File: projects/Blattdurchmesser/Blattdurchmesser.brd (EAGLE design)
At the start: 100 x 80 mm, 16 parts, among them K1 TX2_RELAY", Q1 ARDUINOR3-NOIOREF-NOTEXT

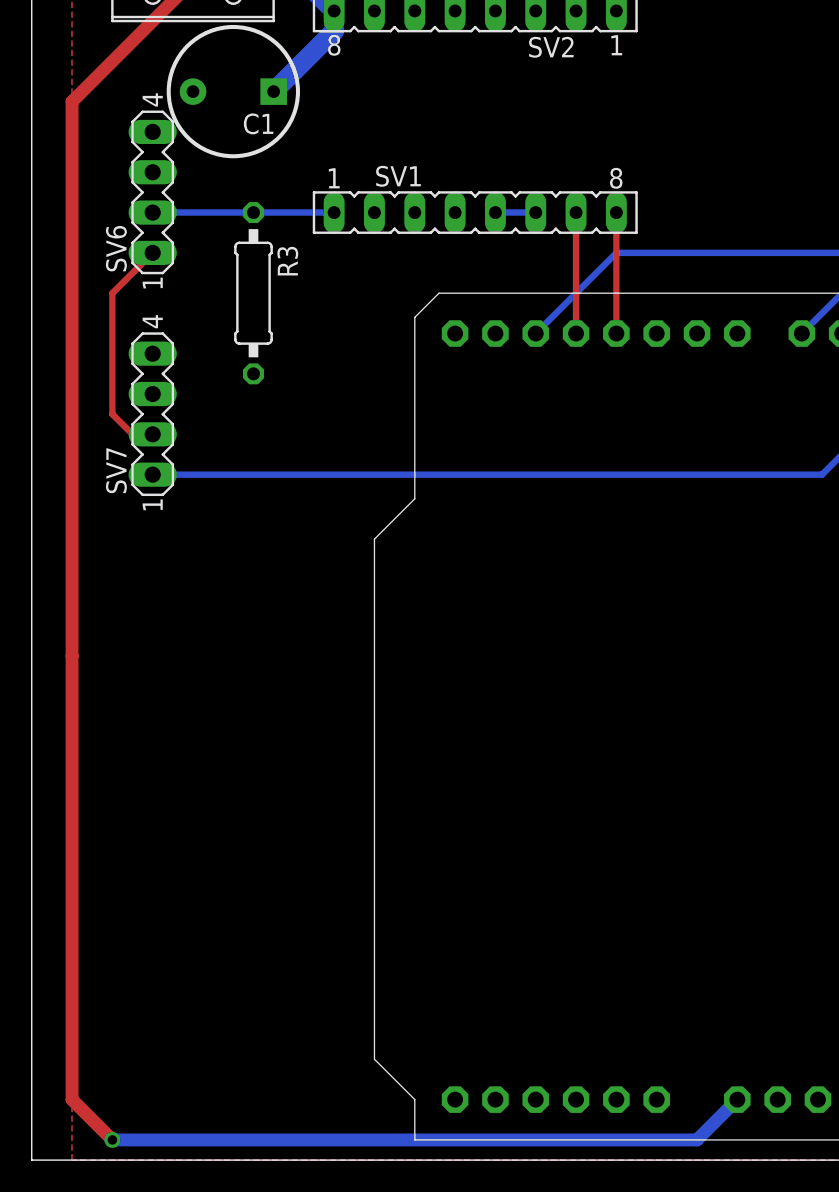
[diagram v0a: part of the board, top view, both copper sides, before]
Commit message: bugfix; * edrc dimension errors
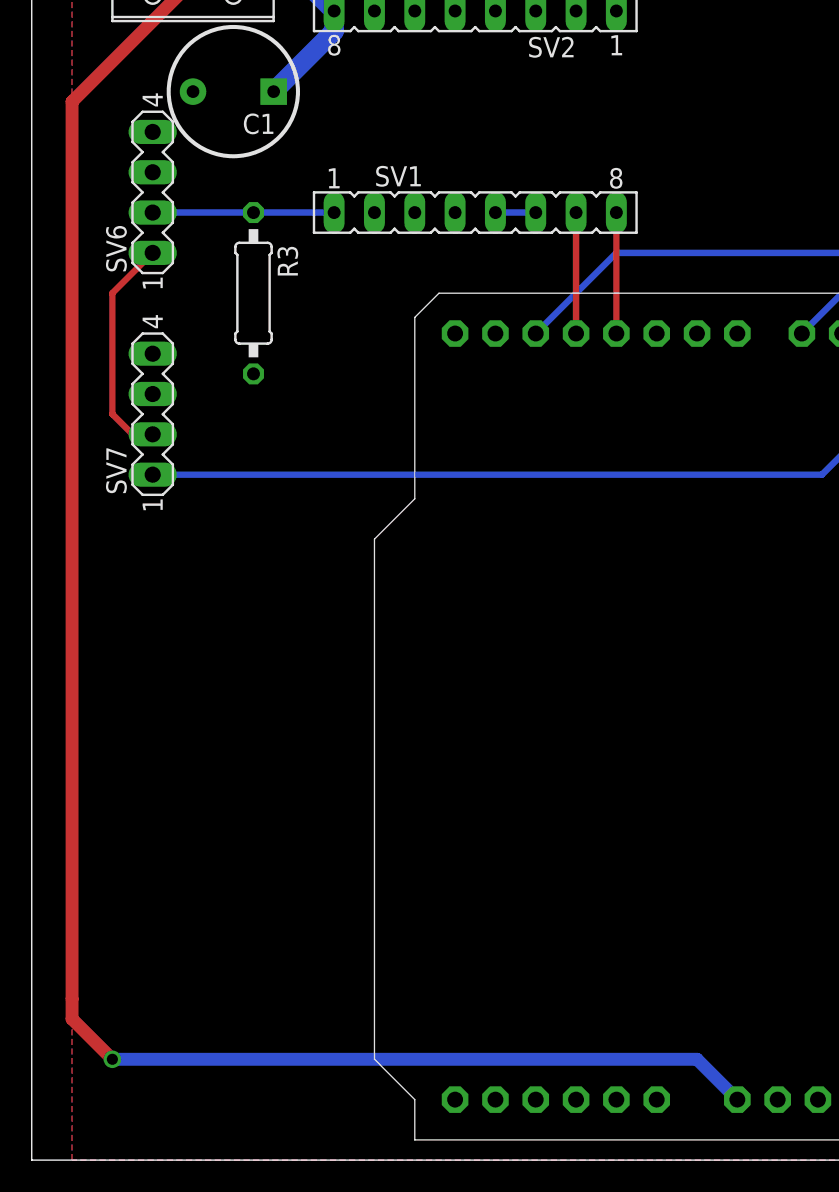
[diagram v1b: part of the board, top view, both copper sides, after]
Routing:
- net +12V: track 136.1 -> 131.0 mm
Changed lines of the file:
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@@
 <wire x1="19.05" y1="72.39" x2="19.05" y2="71.12" width="1.2192" layer="16"/>
 <wire x1="19.05" y1="71.12" x2="15.24" y2="67.31" width="1.2192" layer="16"/>
-<wire x1="2.54" y1="31.75" x2="2.54" y2="66.675" width="0.8128" layer="1"/>
+<wire x1="2.54" y1="10.16" x2="2.54" y2="66.675" width="0.8128" layer="1"/>
 <wire x1="2.54" y1="66.675" x2="12.7" y2="76.835" width="0.8128" layer="1"/>
 <contactref element="Q1" pad="VIN"/>
-<wire x1="2.54" y1="31.75" x2="2.54" y2="3.81" width="0.8128" layer="1"/>
-<wire x1="2.54" y1="3.81" x2="5.08" y2="1.27" width="0.8128" layer="1"/>
-<via x="5.08" y="1.27" extent="1-16" drill="0.6"/>
-<wire x1="5.08" y1="1.27" x2="41.91" y2="1.27" width="0.8128" layer="16"/>
-<wire x1="41.91" y1="1.27" x2="44.45" y2="3.81" width="0.8128" layer="16"/>
+<wire x1="44.45" y1="3.81" x2="41.91" y2="6.35" width="0.8128" layer="16"/>
+<wire x1="41.91" y1="6.35" x2="5.08" y2="6.35" width="0.8128" layer="16"/>
+<via x="5.08" y="6.35" extent="1-16" drill="0.7"/>
+<wire x1="5.08" y1="6.35" x2="2.54" y2="8.89" width="0.8128" layer="1"/>
+<wire x1="2.54" y1="8.89" x2="2.54" y2="10.16" width="0.8128" layer="1"/>
 </signal>
 <signal name="N$3">

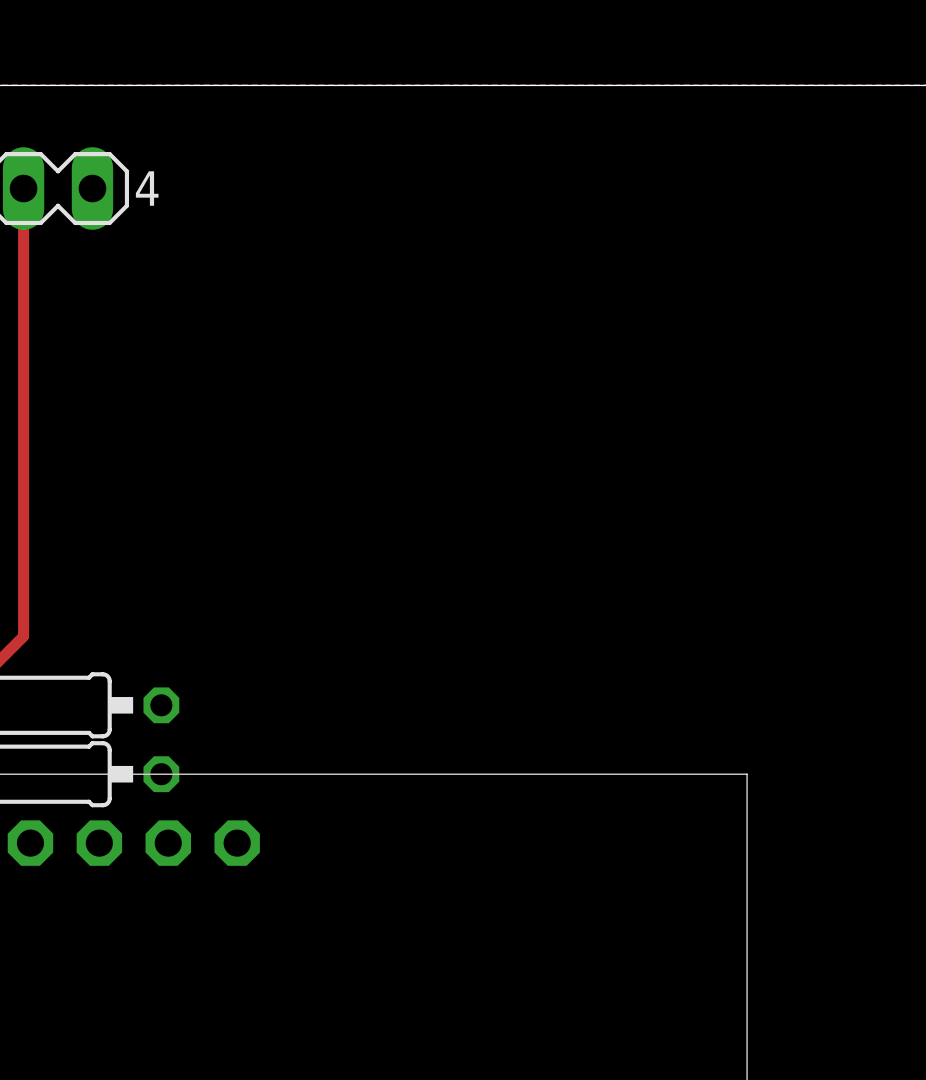
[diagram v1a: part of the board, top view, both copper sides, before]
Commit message: new feature; * add i2c OLED display
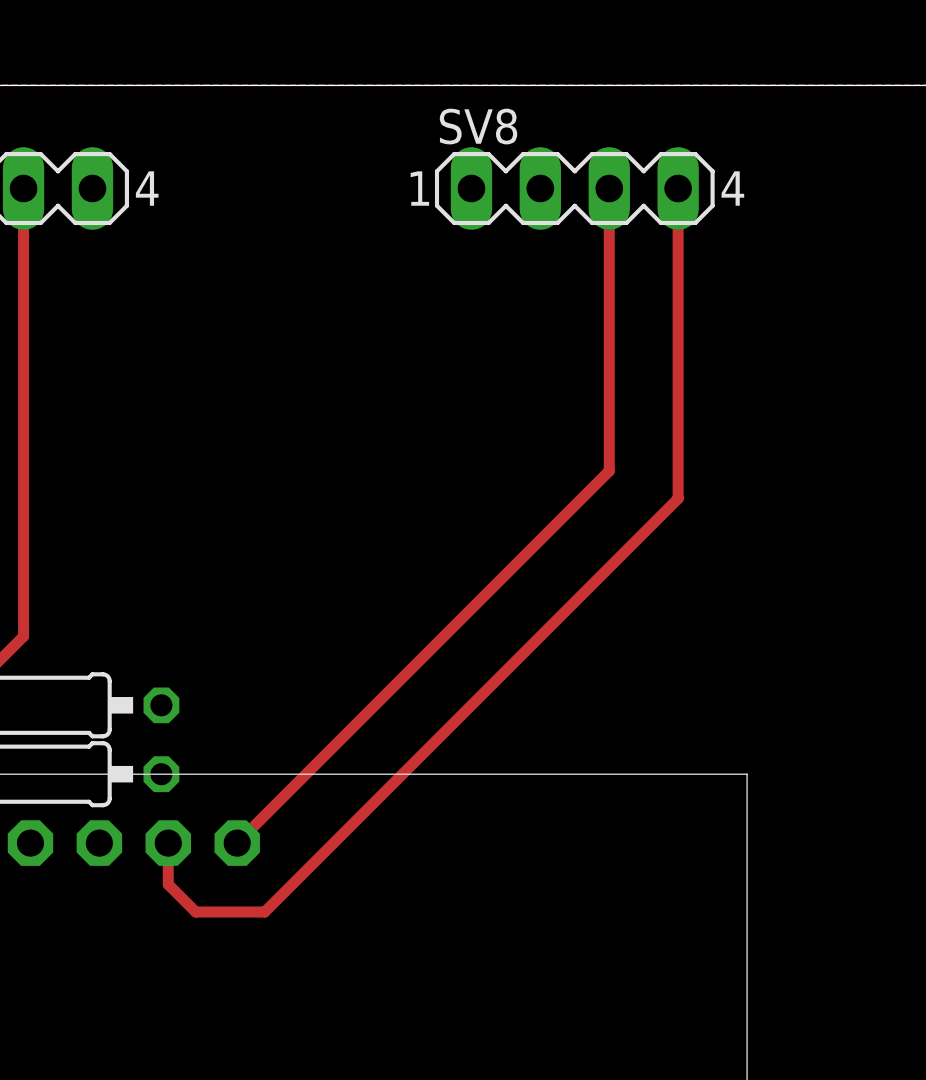
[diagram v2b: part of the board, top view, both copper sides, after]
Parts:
- added SV8: (no value), con-lstb:MA04-1
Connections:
- new net N$17: Q1.SCL, SV8.3
- new net N$18: Q1.SDA, SV8.4
- net +5V: now also SV8.2
- net GND: now also SV8.1
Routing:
- net N$18: track 0.00 -> 38.5 mm
- net N$17: track 0.00 -> 29.8 mm
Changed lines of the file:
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@@
 <attribute name="MF" value="" x="10.16" y="76.2" size="1.778" layer="27" rot="R180" display="off"/>
+</element>
+<element name="SV8" library="con-lstb" package="MA04-1" value="" x="83.82" y="76.2">
+<attribute name="MPN" value="" x="83.82" y="76.2" size="1.778" layer="27" display="off"/>
+<attribute name="OC_FARNELL" value="unknown" x="83.82" y="76.2" size="1.778" layer="27" display="off"/>
+<attribute name="MF" value="" x="83.82" y="76.2" size="1.778" layer="27" display="off"/>
+<attribute name="OC_NEWARK" value="unknown" x="83.82" y="76.2" size="1.778" layer="27" display="off"/>
 </element>
 </elements>
@@
 <contactref element="Q1" pad="GND"/>
 <contactref element="X1" pad="2"/>
+<contactref element="SV8" pad="1"/>
 </signal>
 <signal name="GND1">
@@
 <contactref element="R3" pad="2"/>
 <contactref element="Q1" pad="5V"/>
+<contactref element="SV8" pad="2"/>
 </signal>
 <signal name="+12V">
@@
 <wire x1="6.35" y1="45.72" x2="5.08" y2="46.99" width="0.4064" layer="1"/>
 </signal>
+<signal name="N$17">
+<contactref element="SV8" pad="3"/>
+<contactref element="Q1" pad="SCL"/>
+<wire x1="85.09" y1="76.2" x2="85.09" y2="65.786" width="0.4064" layer="1"/>
+<wire x1="85.09" y1="65.786" x2="71.374" y2="52.07" width="0.4064" layer="1"/>
+</signal>
+<signal name="N$18">
+<contactref element="SV8" pad="4"/>
+<contactref element="Q1" pad="SDA"/>
+<wire x1="87.63" y1="76.2" x2="87.63" y2="64.77" width="0.4064" layer="1"/>
+<wire x1="87.63" y1="64.77" x2="72.39" y2="49.53" width="0.4064" layer="1"/>
+<wire x1="72.39" y1="49.53" x2="69.85" y2="49.53" width="0.4064" layer="1"/>
+<wire x1="69.85" y1="49.53" x2="68.834" y2="50.546" width="0.4064" layer="1"/>
+<wire x1="68.834" y1="50.546" x2="68.834" y2="52.07" width="0.4064" layer="1"/>
+</signal>
 </signals>

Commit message: improvement; * rearranged schematic              * rearranged pcb
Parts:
- moved SV5 17.8 mm to (66.0, 76.2)
- moved SV4 10.2 mm to (52.1, 76.2)
- moved R1 7.62 mm to (55.9, 57.1)
- moved R2 7.62 mm to (55.9, 54.6)
- moved SV8 3.81 mm to (80.0, 76.2)
- moved R3 1.27 mm to (12.7, 54.6)
- moved SV6 1.27 mm to (6.35, 61.0)
- moved SV7 1.27 mm to (6.35, 47.0)
- moved C1 1.27 mm to (14.0, 66.0)
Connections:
- net N$15: now also Q1.A0
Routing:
- net N$15: track 48.9 -> 91.6 mm
- net N$13: track 24.6 -> 36.2 mm, vias 0 -> 1
- net N$9: track 34.7 -> 26.1 mm
- net N$12: track 35.8 -> 28.8 mm
- net N$18: track 38.5 -> 36.9 mm
- net N$17: track 29.8 -> 28.2 mm
- net N$14: track 11.4 -> 12.7 mm
- net N$11: track 54.7 -> 56.0 mm
- net +12V: track 131.0 -> 132.3 mm

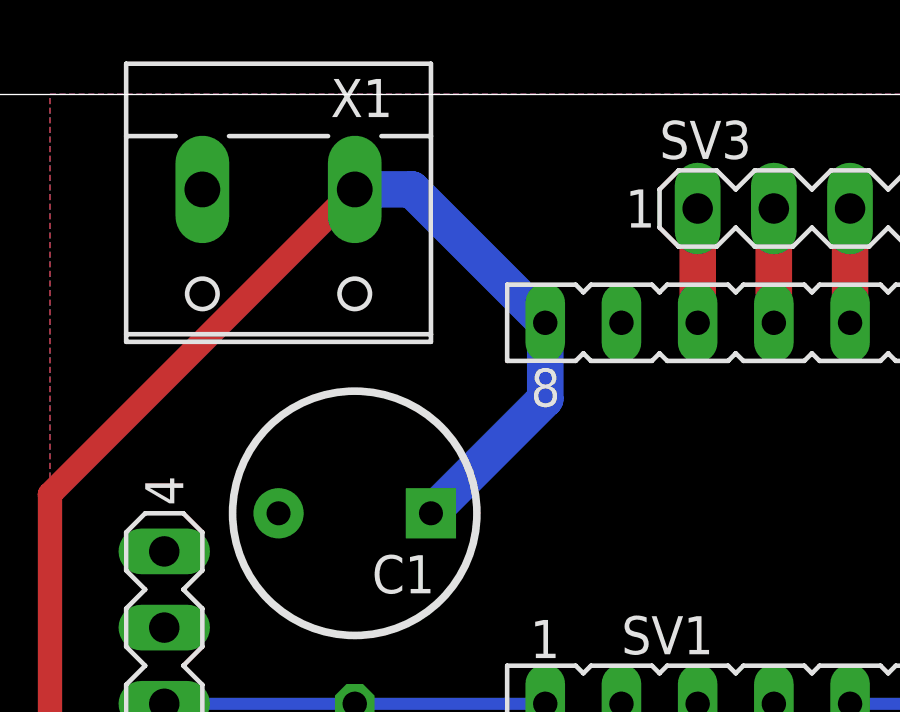
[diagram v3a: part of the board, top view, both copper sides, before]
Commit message: improvement; * move stepper power line to top plane              * add labels to connectors
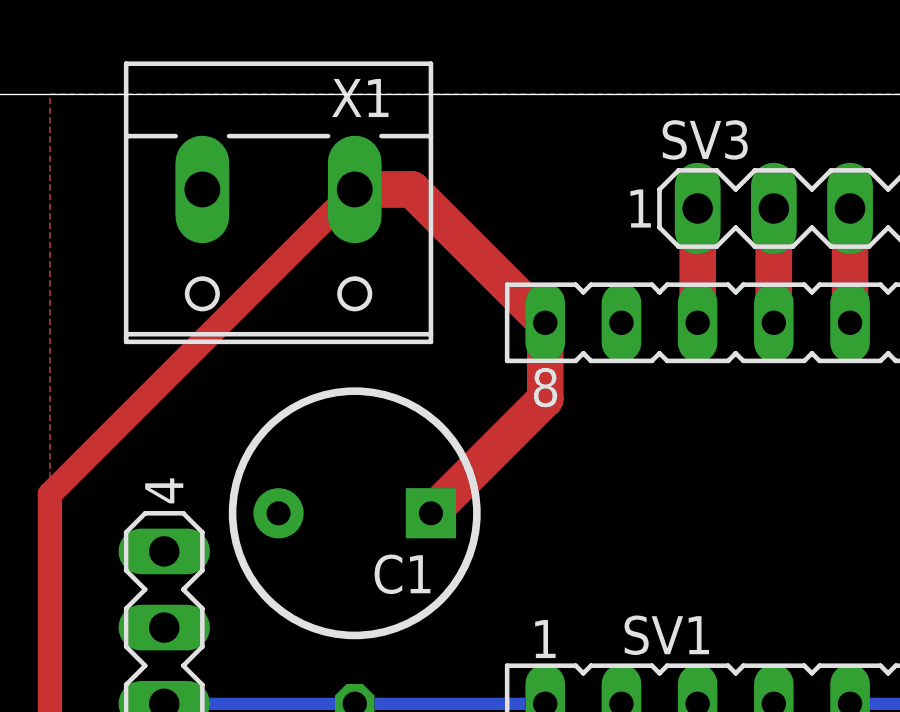
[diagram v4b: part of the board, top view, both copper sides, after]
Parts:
- SV1, SV2: value (none) -> A4988
- SV3: value (none) -> stepper
- SV4: value (none) -> optical
- SV5: value (none) -> mechanical
- SV6: value (none) -> protect2
- SV7: value (none) -> protect1
- SV8: value (none) -> OLED
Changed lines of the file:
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@@
 <elements>
 <element name="K1" library="relay" package="TX2" value="TX2_RELAY&quot;" x="72.39" y="17.78"/>
-<element name="SV1" library="con-lsta" package="FE08" value="" x="27.94" y="59.69">
+<element name="SV1" library="con-lsta" package="FE08" value="A4988" x="27.94" y="59.69">
 <attribute name="MPN" value="" x="27.94" y="59.69" size="1.778" layer="27" display="off"/>
 <attribute name="OC_NEWARK" value="unknown" x="27.94" y="59.69" size="1.778" layer="27" display="off"/>
@@
 <attribute name="MF" value="" x="27.94" y="59.69" size="1.778" layer="27" display="off"/>
 </element>
-<element name="SV2" library="con-lsta" package="FE08" value="" x="27.94" y="72.39" rot="R180">
+<element name="SV2" library="con-lsta" package="FE08" value="A4988" x="27.94" y="72.39" rot="R180">
 <attribute name="MPN" value="" x="27.94" y="72.39" size="1.778" layer="27" rot="R180" display="off"/>
 <attribute name="OC_NEWARK" value="unknown" x="27.94" y="72.39" size="1.778" layer="27" rot="R180" display="off"/>
@@
 <attribute name="MF" value="" x="27.94" y="72.39" size="1.778" layer="27" rot="R180" display="off"/>
 </element>
-<element name="SV4" library="con-lstb" package="MA04-1" value="" x="52.07" y="76.2">
+<element name="SV4" library="con-lstb" package="MA04-1" value="optical" x="52.07" y="76.2">
 <attribute name="MPN" value="" x="52.07" y="76.2" size="1.778" layer="27" display="off"/>
 <attribute name="OC_NEWARK" value="unknown" x="52.07" y="76.2" size="1.778" layer="27" display="off"/>
@@
 <attribute name="MF" value="" x="66.04" y="27.94" size="1.778" layer="27" display="off"/>
 </element>
-<element name="SV3" library="con-lstb" package="MA04-1" value="" x="27.94" y="76.2">
+<element name="SV3" library="con-lstb" package="MA04-1" value="stepper" x="27.94" y="76.2">
 <attribute name="MPN" value="" x="27.94" y="76.2" size="1.778" layer="27" display="off"/>
 <attribute name="OC_NEWARK" value="unknown" x="27.94" y="76.2" size="1.778" layer="27" display="off"/>
@@
 </element>
 <element name="C1" library="Elkos" package="R_ELK_8.1" value="R_ELKO_8.1" x="13.97" y="66.04" rot="R180"/>
-<element name="SV5" library="con-lstb" package="MA04-1" value="" x="66.04" y="76.2">
+<element name="SV5" library="con-lstb" package="MA04-1" value="mechanical" x="66.04" y="76.2">
 <attribute name="MPN" value="" x="66.04" y="76.2" size="1.778" layer="27" display="off"/>
 <attribute name="OC_NEWARK" value="unknown" x="66.04" y="76.2" size="1.778" layer="27" display="off"/>
@@
 <element name="R1" library="rcl" package="0207/10" value="1k" x="55.88" y="57.15"/>
 <element name="R2" library="rcl" package="0207/10" value="1k" x="55.88" y="54.61"/>
-<element name="SV6" library="con-lstb" package="MA04-1" value="" x="6.35" y="60.96" rot="R90">
+<element name="SV6" library="con-lstb" package="MA04-1" value="protect2" x="6.35" y="60.96" rot="R90">
 <attribute name="MPN" value="" x="6.35" y="60.96" size="1.778" layer="27" rot="R90" display="off"/>
 <attribute name="OC_NEWARK" value="unknown" x="6.35" y="60.96" size="1.778" layer="27" rot="R90" display="off"/>
@@
 <element name="R3" library="rcl" package="0207/10" value="4.7k" x="12.7" y="54.61" rot="R270"/>
 <element name="Q1" library="adafruit" package="ARDUINOR3-NOTEXT-NOIOREF" value="ARDUINOR3-NOIOREF-NOTEXT" x="90.17" y="1.27" rot="MR0"/>
-<element name="SV7" library="con-lstb" package="MA04-1" value="" x="6.35" y="46.99" rot="R90">
+<element name="SV7" library="con-lstb" package="MA04-1" value="protect1" x="6.35" y="46.99" rot="R90">
 <attribute name="MPN" value="" x="6.35" y="46.99" size="1.778" layer="27" rot="R90" display="off"/>
 <attribute name="OC_FARNELL" value="unknown" x="6.35" y="46.99" size="1.778" layer="27" rot="R90" display="off"/>
@@
 <attribute name="MF" value="" x="10.16" y="76.2" size="1.778" layer="27" rot="R180" display="off"/>
 </element>
-<element name="SV8" library="con-lstb" package="MA04-1" value="" x="80.01" y="76.2">
+<element name="SV8" library="con-lstb" package="MA04-1" value="OLED" x="80.01" y="76.2">
 <attribute name="MPN" value="" x="80.01" y="76.2" size="1.778" layer="27" display="off"/>
 <attribute name="OC_FARNELL" value="unknown" x="80.01" y="76.2" size="1.778" layer="27" display="off"/>
@@
 <contactref element="C1" pad="P"/>
 <contactref element="X1" pad="1"/>
-<wire x1="12.7" y1="76.835" x2="14.605" y2="76.835" width="1.2192" layer="16"/>
-<wire x1="14.605" y1="76.835" x2="19.05" y2="72.39" width="1.2192" layer="16"/>
-<wire x1="19.05" y1="72.39" x2="19.05" y2="69.85" width="1.2192" layer="16"/>
-<wire x1="19.05" y1="69.85" x2="15.24" y2="66.04" width="1.2192" layer="16"/>
+<wire x1="12.7" y1="76.835" x2="14.605" y2="76.835" width="1.2192" layer="1"/>
+<wire x1="14.605" y1="76.835" x2="19.05" y2="72.39" width="1.2192" layer="1"/>
+<wire x1="19.05" y1="72.39" x2="19.05" y2="69.85" width="1.2192" layer="1"/>
+<wire x1="19.05" y1="69.85" x2="15.24" y2="66.04" width="1.2192" layer="1"/>
 <wire x1="2.54" y1="8.89" x2="2.54" y2="66.675" width="0.8128" layer="1"/>
 <wire x1="2.54" y1="66.675" x2="12.7" y2="76.835" width="0.8128" layer="1"/>
